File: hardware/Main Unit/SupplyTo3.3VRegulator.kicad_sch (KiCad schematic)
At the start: 18 parts, among them U11 TPS56A37RPAR, U12 INA180A3

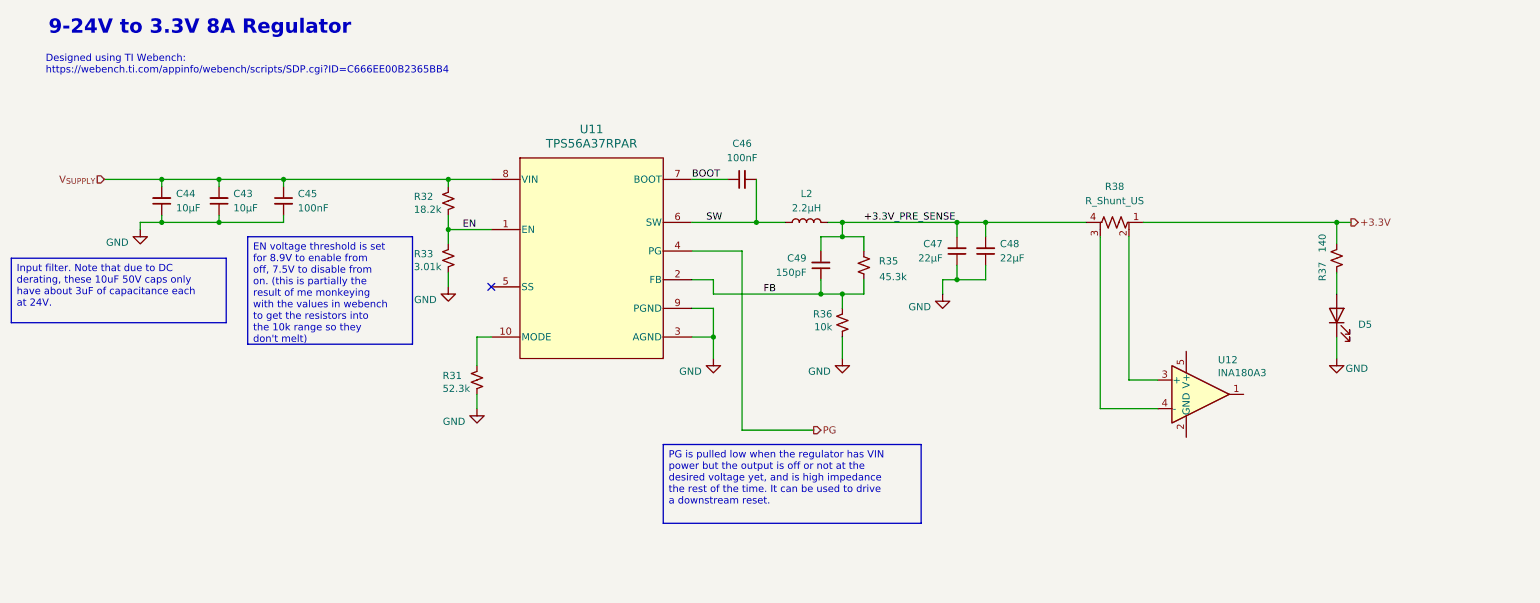
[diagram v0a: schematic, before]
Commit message: Finish 3.3V regulator
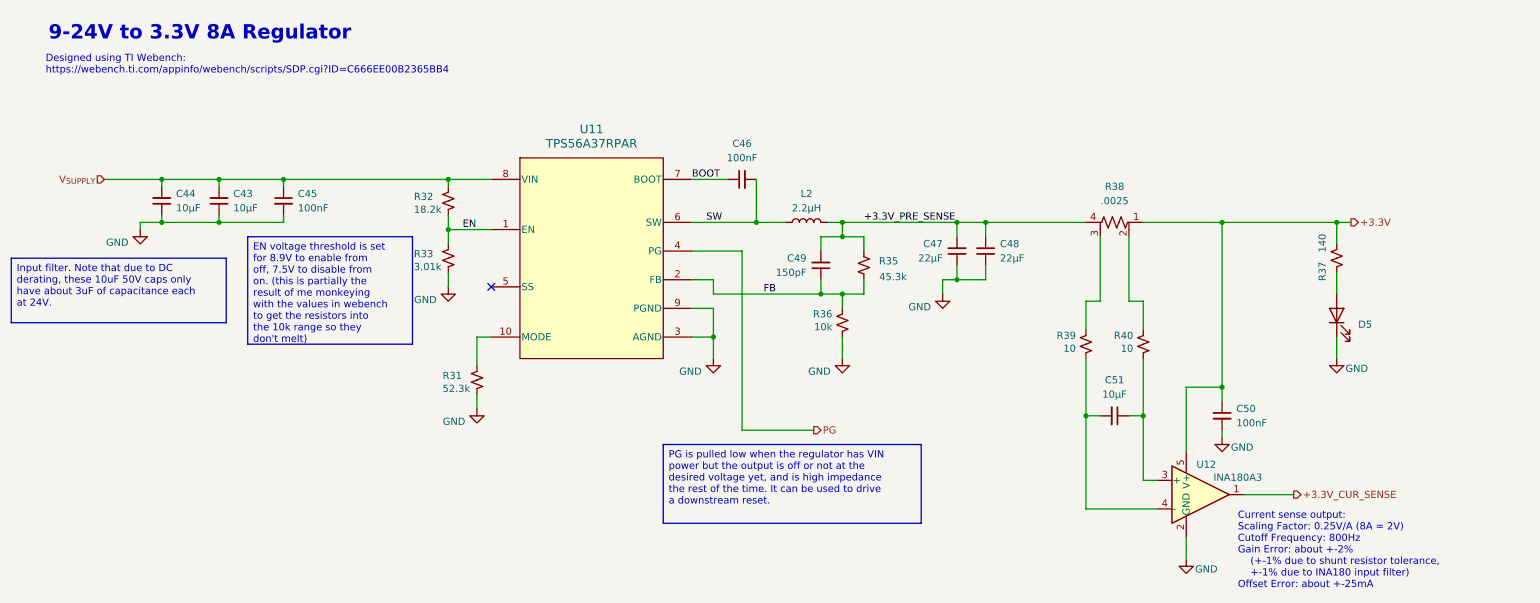
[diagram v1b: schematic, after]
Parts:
- added C50: 100nF, Capacitor_SMD:C_0603_1608Metric, symbol Device:C_Small
- added C51: 10µF, Capacitor_SMD:C_1206_3216Metric, symbol Device:C_Small
- added R39, R40: 10, Resistor_SMD:R_0603_1608Metric, symbol Device:R_Small_US
- R38: value R_Shunt_US -> .0025; footprint (none) -> Project Library:D1FCP0612; LibRef (none) -> D1FCP0612D2M50FF-T5; SKU (none) -> 4463-D1FCP0612D2M50FF-T5CT-ND; Supplier (none) -> Digi-Key
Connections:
- net +3.3V: now also U12.5 (V+), C50.1
- net GND: now also U12.2 (GND), C50.2
- net at R38.2: now also R40.1; no longer U12.3 (+)
- net at R38.3: now also R39.1; no longer U12.4 (-)
- net +3.3V_CUR_SENSE: now reaches U12.1
- new net: C51.1, R40.2, U12.3 (+)
- new net: C51.2, R39.2, U12.4 (-)
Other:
- note added: "Current sense output: Scaling Factor: 0.25V/A (8A = 2V) Cutoff Frequency: 800Hz Gain Error: about +-2% (+-1% due to shunt resistor tolerance, +-1% due to INA180 input filter) Offset Error: about +-25mA"
- moved on the sheet: U12

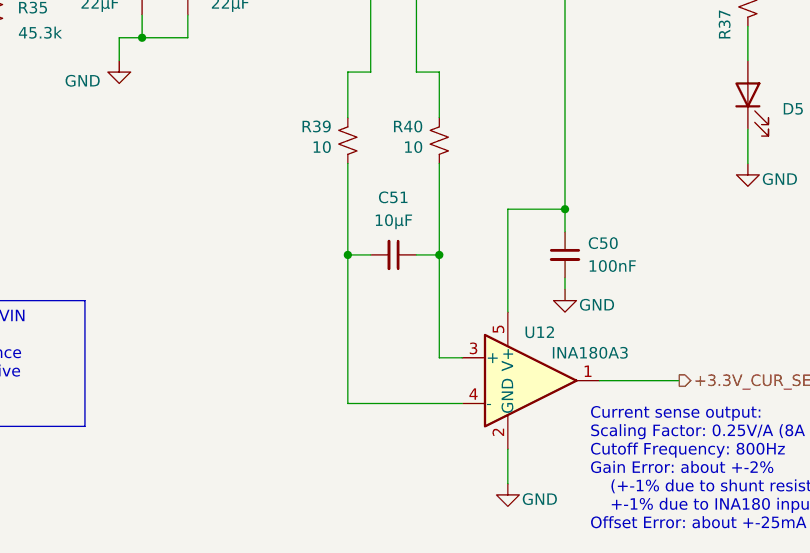
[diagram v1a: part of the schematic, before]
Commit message: Add schematic for Vsupply input
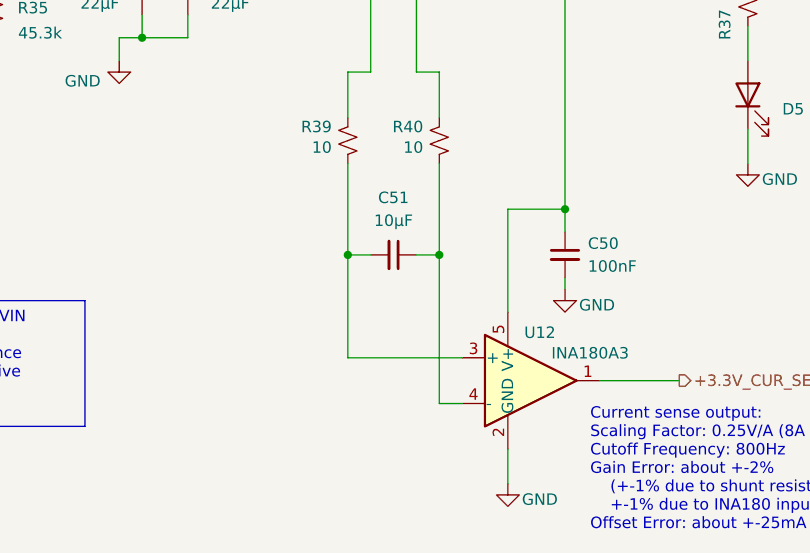
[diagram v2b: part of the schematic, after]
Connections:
- net at C51.1, R40.2: now also U12.4 (-); no longer U12.3 (+)
- net at C51.2, R39.2: now also U12.3 (+); no longer U12.4 (-)
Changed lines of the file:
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@@
+	)
+	(junction
+		(at 59.69 60.96)
+		(diameter 0)
+		(color 0 0 0 0)
+	)
+	(junction
+		(at 237.49 97.79)
+		(diameter 0)
+		(color 0 0 0 0)
+	)
+	(junction
+		(at 147.32 88.9)
+		(diameter 0)
+		(color 0 0 0 0)
+	)
+	(junction
+		(at 49.53 68.58)
+		(diameter 0)
+		(color 0 0 0 0)
 	)
 	(junction
@@
 	)
 	(junction
-		(at 59.69 60.96)
-		(diameter 0)
-		(color 0 0 0 0)
-	)
-	(junction
-		(at 237.49 97.79)
-		(diameter 0)
-		(color 0 0 0 0)
-	)
-	(junction
-		(at 147.32 88.9)
-		(diameter 0)
-		(color 0 0 0 0)
-	)
-	(junction
-		(at 49.53 68.58)
-		(diameter 0)
-		(color 0 0 0 0)
-	)
-	(junction
 		(at 170.18 71.12)
 		(diameter 0)
@@
 	)
 	(junction
+		(at 223.52 102.87)
+		(diameter 0)
+		(color 0 0 0 0)
+	)
+	(junction
 		(at 71.12 60.96)
 		(diameter 0)
@@
 	(junction
 		(at 170.18 81.28)
-		(diameter 0)
-		(color 0 0 0 0)
-	)
-	(junction
-		(at 223.52 102.87)
 		(diameter 0)
 		(color 0 0 0 0)
@@
 	(wire
 		(pts
+			(xy 223.52 102.87) (xy 223.52 119.38)
+		)
+		(stroke
+			(width 0)
+			(type default)
+		)
+	)
+	(wire
+		(pts
 			(xy 223.52 82.55) (xy 220.98 82.55)
 		)
@@
 	(wire
 		(pts
+			(xy 213.36 114.3) (xy 213.36 102.87)
+		)
+		(stroke
+			(width 0)
+			(type default)
+		)
+	)
+	(wire
+		(pts
 			(xy 143.51 88.9) (xy 147.32 88.9)
 		)
@@
 	(wire
 		(pts
-			(xy 213.36 119.38) (xy 213.36 102.87)
-		)
-		(stroke
-			(width 0)
-			(type default)
-		)
-	)
-	(wire
-		(pts
 			(xy 170.18 88.9) (xy 170.18 92.71)
 		)
@@
 	(wire
 		(pts
-			(xy 223.52 114.3) (xy 223.52 102.87)
-		)
-		(stroke
-			(width 0)
-			(type default)
-		)
-	)
-	(wire
-		(pts
 			(xy 237.49 97.79) (xy 237.49 100.33)
 		)
@@
 	(wire
 		(pts
-			(xy 223.52 102.87) (xy 223.52 92.71)
-		)
-		(stroke
-			(width 0)
-			(type default)
-		)
-	)
-	(wire
-		(pts
 			(xy 100.33 69.85) (xy 107.95 69.85)
 		)
@@
 	(wire
 		(pts
+			(xy 223.52 92.71) (xy 223.52 102.87)
+		)
+		(stroke
+			(width 0)
+			(type default)
+		)
+	)
+	(wire
+		(pts
 			(xy 257.81 77.47) (xy 257.81 81.28)
 		)
@@
 	(wire
 		(pts
-			(xy 226.06 119.38) (xy 213.36 119.38)
+			(xy 223.52 119.38) (xy 226.06 119.38)
 		)
 		(stroke
@@
 	(wire
 		(pts
+			(xy 213.36 114.3) (xy 226.06 114.3)
+		)
+		(stroke
+			(width 0)
+			(type default)
+		)
+	)
+	(wire
+		(pts
 			(xy 154.94 60.96) (xy 154.94 68.58)
 		)
@@
 		)
 		(stroke
-			(width 0)
-			(type default)
-		)
-	)
-	(wire
-		(pts
-			(xy 226.06 114.3) (xy 223.52 114.3)
-		)
-		(stroke
